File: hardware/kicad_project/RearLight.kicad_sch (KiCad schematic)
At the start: 54 parts, among them J1 USB_C_Receptacle_USB2.0_16P, J2 Conn_02x03_Odd_Even, Q1 CSD16404Q5A, Q2 CSD16404Q5A, U1 453-00039R, U2 USBLC6-2SC6, U3 NPM1100-CAAB-R, U4 DW01A, U5 LIS3DH, U6 OPT3001DNPR, U8 PAM2804AAB010

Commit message: Schematic done; Layout first draft
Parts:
- removed BT1: Battery_Cell, symbol Device:Battery_Cell
- removed D1: L0805G, Capacitor_SMD:C_0805_2012Metric_Pad1.18x1.45mm_HandSolder, symbol Device:LED
- removed D2: L0805R, Capacitor_SMD:C_0805_2012Metric_Pad1.18x1.45mm_HandSolder, symbol Device:LED
- removed D3: XPEBRD-L1, LED_SMD:LED_Cree-XP, symbol RearLight:XPEBRD-L1-0000-00901
- removed MH1, MH2, MH3, MH4: M3, MountingHole:MountingHole_3.2mm_M3_Pad_Via, symbol Mechanical:MountingHole_Pad
- removed Q1, Q2: CSD16404Q5A, Package_TO_SOT_SMD:TDSON-8-1, symbol Transistor_FET:CSD16404Q5A
- removed R16: 2, Resistor_SMD:R_0603_1608Metric, symbol Device:R
- removed R17, R18: 1, Resistor_SMD:R_0603_1608Metric, symbol Device:R
- removed U3: NPM1100-CAAB-R, RearLight:BGA25C40P5X5_207X207X52N, symbol RearLight:NPM1100-CAAB-R
- added BT1: 1096, RearLight:BAT_1096_holes_slim, symbol RearLight:1096
- added C15: 100n, Capacitor_SMD:C_0805_2012Metric, symbol Device:C
- added H1, H2, H3, H4: M2, MountingHole:MountingHole_2.1mm, symbol Mechanical:MountingHole
- added LED1: XPEBRD-L1-0000-00801, RearLight:XPEWHTL1000000E01, symbol RearLight:XPEBRD-L1-0000-00801
- added LED2: LTRB_RASF.01-6B6C-C3E6-0-0-R18, RearLight:LTRBRASF016B6CC3E600R18, symbol RearLight:LTRB_RASF.01-6B6C-C3E6-0-0-R18
- added Q1, Q3: AO3400A, Package_TO_SOT_SMD:SOT-23, symbol Transistor_FET:AO3400A
- added R10: 49R9, Resistor_SMD:R_0402_1005Metric, symbol Device:R
- added R19: 100, Resistor_SMD:R_0402_1005Metric, symbol Device:R
- added R9: 0R1, Resistor_SMD:R_1206_3216Metric, symbol Device:R
- added SW1: SW_Push, RearLight:SW_TS-1088-AR02016, symbol Switch:SW_Push
- added U7: NPM1100-QDAB-R, RearLight:QFN50P400X400X90-25N-D, symbol RearLight:NPM1100-QDAB-R
- C1: Manufacturer Part Number CL21A475KAQNNNE -> (none); manf# (none) -> CL21A475KAQNNNE
- C10, C11, C13, C14, C8, C9: Manufacturer Part Number CL21A106KAYNNNE -> (none); manf# (none) -> CL21A106KAYNNNE
- C12, C5, C6, C7: Manufacturer Part Number CL21B104KCFNNNE -> (none); manf# (none) -> CL21B104KCFNNNE
- C2, C3: Manufacturer Part Number CL10B474KA8NNNC -> (none); manf# (none) -> CL10B474KA8NNNC
- C4: Manufacturer Part Number CL21A225KBQNNNE -> (none); manf# (none) -> CL21A225KBQNNNE
- J1: footprint Connector_USB:USB_C_Receptacle_GCT_USB4105-xx-A_16P_TopMnt_Horizontal -> Connector_USB:USB_C_Receptacle_GCT_USB4105-xx-A_16P_TopMnt_Horizontal_wide_slot; Distribution Link 1 (none) -> https://jlcpcb.com/partdetail/3554049-USB4105_GF_A060/C3025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; LCSC (none) -> C3025063; Manufacturer (none) -> Global Connector Technology; Manufacturer Part Number (none) -> USB4105-GF-A-060; manf# (none) -> USB4105-GF-A-060; now left out of the parts list
- J2: now not fitted
- L1, L2: Manufacturer Part Number CMI201209U2R2KT -> (none); manf# (none) -> CMI201209U2R2KT
- R1, R5: Manufacturer Part Number 0603WAF0000T5E -> (none); manf# (none) -> 0603WAF0000T5E
- R11: Distribution Link 1 https://eu.mouser.com/ProductDetail/Royalohm/0603WAF0000T5E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 -> https://jlcpcb.com/partdetail/26547-0603WAF1002T5E/C25804; Distribution Link 2 https://www.lcsc.com/product-detail/C21189.html -> (none); LCSC C21189 -> C25804; manf# (none) -> 0603WAF1002T5E
- R12, R13, R14, R2, R6: footprint Resistor_SMD:R_0603_1608Metric -> Resistor_SMD:R_0402_1005Metric; Distribution Link 1 https://eu.mouser.com/ProductDetail/Royalohm/0603WAF0000T5E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 -> https://jlcpcb.com/partdetail/26487-0402WGF1002TCE/C25744; Distribution Link 2 https://www.lcsc.com/product-detail/C21189.html -> (none); LCSC C21189 -> C25744; Manufacturer Part Number 0603WAF1002T5E -> 0402WGF1002TCE; manf# (none) -> 0402WGF1002TCE
- R15: value 1 -> 0R1; footprint Resistor_SMD:R_0603_1608Metric -> Resistor_SMD:R_1206_3216Metric; Distribution Link 1 https://www.mouser.com/ProductDetail/Royalohm/0603WAF100KT5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 -> https://jlcpcb.com/partdetail/26077-1206W4F100LT5E/C25334; Distribution Link 2 https://www.lcsc.com/product-detail/C22936.html -> (none); LCSC C22936 -> C25334; Manufacturer Part Number 0603WAF100KT5E -> 1206W4F100LT5E; manf# (none) -> 1206W4F100LT5E
- R3: footprint Resistor_SMD:R_0603_1608Metric -> Resistor_SMD:R_0402_1005Metric; Distribution Link 1 https://jlcpcb.com/partdetail/23906-0603WAF4700T5E/C23179 -> https://jlcpcb.com/partdetail/25860-0402WGF4700TCE/C25117; Distribution Link 2 https://www.lcsc.com/product-detail/C23179.html?s_z=n_C23179 -> (none); Manufacturer Part Number 0603WAF4700T5E -> 0402WGF4700TCE; manf# (none) -> 0402WGF4700TCE
- R4: footprint Resistor_SMD:R_0603_1608Metric -> Resistor_SMD:R_0402_1005Metric; Distribution Link 1 https://www.lcsc.com/product-detail/C22975.html?s_z=n_C22975 -> https://jlcpcb.com/partdetail/4516-0402WGF2001TCE/C4109; Distribution Link 2 https://jlcpcb.com/partdetail/23702-0603WAF2001T5E/C22975 -> (none); LCSC C22975 -> C4109; Manufacturer Part Number 0603WAF2001T5E -> 0402WGF2001TCE; manf# (none) -> 0402WGF2001TCE
- R7, R8: footprint Resistor_SMD:R_0603_1608Metric -> Resistor_SMD:R_0402_1005Metric; LCSC C23186 -> C25905; Manufacturer Part Number 0603WAF5101T5E -> 0402WGF5101TCE; manf# (none) -> 0402WGF5101TCE
- U1: footprint RF_Module:Laird_BL653 -> Liard_BL653_ 453-00039_Custom:Laird_BL653; manf# (none) -> 453-00039R
- U4: Manufacturer Part Number DW01A -> (none); manf# (none) -> DW01A
- U5: Manufacturer Part Number LIS3DHTR -> (none); manf# (none) -> LIS3DHTR
- U6: Manufacturer Part Number OPT3001DNPR -> (none); manf# (none) -> OPT3001DNPR
- U8: Manufacturer Part Number PAM2804AAB010 -> (none); manf# (none) -> PAM2804AAB010
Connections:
- net +BATT: now also C14.1, U8.4 (VIN), BT1.P, U7.15 (VBAT)
- net +VBUS_FIL: now also U7.17 (VBUS)
- net +VDD_nRF: now also LED2.3 (A_BLUE), R10.1, R19.1, U7.1 (VOUTB); no longer C14.1, U8.4 (VIN)
- net +VSYS: now also U7.16 (VSYS), U7.2 (VOUTBSET1), U7.5 (ISET), U7.9 (VTERMSET); no longer C8.1
- net GND: now also C15.2, LED1.3 (THERMAL_PAD), Q1.2 (S), SW1.2, U7.11 (SHPHLD), U7.19 (D-), U7.23 (PVSS), U7.25 (AVSS), U7.3 (VOUTBSET0), U7.4 (AVSS), U7.6 (SHPACT), U7.7 (MODE)
- net I2C_SCL: now also R12.2; no longer R14.2
- net I2C_SDA: now also R14.2; no longer R12.2
- net at U8.5 (VOUT/FB): now also LED1.1 (K), R9.1; no longer R15.1
- net at C13.1, L2.1: now also LED1.2 (A)
- net at U4.3 (OC): now also Q1.1 (G)
- net at C7.1, R6.2, U1.19 (nRESET): now also J2.3 (Pin_3); no longer J2.4 (Pin_4)
- net at R5.1: now also U7.12 (ICHG)
- net RGB_B: now reaches U1.22 (SIO_14)
- net RGB_B: now also LED2.4 (K_BLUE)
- net RGB_R: now reaches U1.27 (SIO_11)
- net RGB_R: now also LED2.5 (K_RED)
- net RGB_G: now reaches U1.28 (SIO_12)
- net RGB_G: now also LED2.6 (K_GREEN)
- net at U1.59 (NFC1/SIO_09): now also U8.1 (EN)
- net ERR_SIG: now reaches U1.63 (SIO_38)
- net ERR_SIG: now also U7.10 (ERR)
- net CHG_SIG: now reaches U1.64 (SIO_39)
- net CHG_SIG: now also U7.8 (CHG); no longer U8.1 (EN)
- net SWITCH: now reaches U1.7 (SIO_32)
- net SWITCH: now also C15.1, SW1.1
- net at C5.2, U4.6 (GND): now also BT1.N, Q3.2 (S)
- net at L1.2: now also U7.22 (SW)
- net at R2.1: now also U7.14 (NTC)
- net at U4.1 (OD): now also Q3.1 (G)
- new net: R15.1, R9.2
- new net: C8.1, U7.21 (DEC)
- new net: Q1.3 (D), Q3.3 (D)
- new net: LED2.1 (A_GREEN), R10.2
- new net: LED2.2 (A_RED), R19.2
- no-connect marks 51 -> 44
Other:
- note added: "I_LED = 0.1/R_s 0.2 Ω equivalent to get 500mA"
- note removed: "0.285 Ω equivalent to get 350mA"
- note removed: "Unpopulated"
- moved on the sheet: C10, C13, C14, C5, C9, L2, R3, R4, U4, U8

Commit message: Layout 2nd draft
Todo: increase via size
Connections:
- net GND: no longer U1.33 (GND), U1.47 (GND)
- no-connect marks 44 -> 47
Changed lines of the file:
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@@
-	)
-	(junction
-		(at 157.48 124.46)
-		(diameter 0)
-		(color 0 0 0 0)
 	)
 	(junction
@@
 	)
 	(junction
-		(at 165.1 124.46)
-		(diameter 0)
-		(color 0 0 0 0)
-	)
-	(junction
 		(at 273.05 101.6)
 		(diameter 0)
@@
 	)
 	(no_connect
+		(at 157.48 121.92)
+	)
+	(no_connect
 		(at 109.22 96.52)
 	)
@@
 	)
 	(no_connect
+		(at 165.2246 121.92)
+	)
+	(no_connect
 		(at 182.88 99.06)
 	)
@@
 	)
 	(no_connect
+		(at 182.88 73.66)
+	)
+	(no_connect
 		(at 147.32 121.92)
 	)
@@
 	(wire
 		(pts
-			(xy 165.1 124.46) (xy 165.1 121.92)
-		)
-		(stroke
-			(width 0)
-			(type default)
-		)
-	)
-	(wire
-		(pts
 			(xy 134.62 124.46) (xy 137.16 124.46)
 		)
@@
 	(wire
 		(pts
-			(xy 157.48 124.46) (xy 157.48 121.92)
-		)
-		(stroke
-			(width 0)
-			(type default)
-		)
-	)
-	(wire
-		(pts
 			(xy 265.43 36.83) (xy 269.24 36.83)
 		)
@@
 	(wire
 		(pts
-			(xy 165.1 124.46) (xy 167.64 124.46)
-		)
-		(stroke
-			(width 0)
-			(type default)
-		)
-	)
-	(wire
-		(pts
 			(xy 52.07 64.77) (xy 57.15 64.77)
 		)
@@
 	(wire
 		(pts
-			(xy 157.48 124.46) (xy 160.02 124.46)
-		)
-		(stroke
-			(width 0)
-			(type default)
-		)
-	)
-	(wire
-		(pts
 			(xy -44.45 57.15) (xy -44.45 59.69)
 		)
@@
 	(wire
 		(pts
-			(xy 162.56 124.46) (xy 165.1 124.46)
-		)
-		(stroke
-			(width 0)
-			(type default)
-		)
-	)
-	(wire
-		(pts
-			(xy 154.94 124.46) (xy 157.48 124.46)
-		)
-		(stroke
+			(xy 162.56 124.46) (xy 167.64 124.46)
+		)
+		(stroke
+			(width 0)
+			(type default)
+		)
+	)
+	(wire
+		(pts
+			(xy 154.94 124.46) (xy 160.02 124.46)
+		)
+		(stroke

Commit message: DFM design overhaul
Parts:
- removed LED2: LTRB_RASF.01-6B6C-C3E6-0-0-R18, RearLight:LTRBRASF016B6CC3E600R18, symbol RearLight:LTRB_RASF.01-6B6C-C3E6-0-0-R18
- removed R19: 100, Resistor_SMD:R_0402_1005Metric, symbol Device:R
- added D1: LED_R, LED_SMD:LED_0603_1608Metric, symbol Device:LED
- added D2: LED_Y, LED_SMD:LED_0805_2012Metric, symbol Device:LED
- added R16: 49R9, RearLight:R_0402_1005Metric_NO_SILK, symbol Device:R
- BT1, U2, U7: now not fitted; now left out of the parts list
- C2, C3: footprint Capacitor_SMD:C_0603_1608Metric -> RearLight:C_0603_1608Metric_NO_SILK
- FID1, FID2, FID3, H1, H2, H3, H4, J1: now not fitted
- R1, R11, R5: footprint Resistor_SMD:R_0603_1608Metric -> RearLight:R_0603_1608Metric_NO_SILK
- R10, R12, R13, R14, R2, R4, R6, R7, R8: footprint Resistor_SMD:R_0402_1005Metric -> RearLight:R_0402_1005Metric_NO_SILK
- R3: footprint Resistor_SMD:R_0402_1005Metric -> RearLight:R_0402_1005Metric_NO_SILK; LCSC C23179 -> C25117
- U1: footprint Liard_BL653_ 453-00039_Custom:Laird_BL653 -> RF_Module:Laird_BL653; now not fitted; now left out of the parts list
- U5: LCSC (none) -> C15134; Manufacturer Part Number (none) -> LIS3DHTR; now not fitted; now left out of the parts list
- U6: Manufacturer Part Number (none) -> OPT3001DNPR
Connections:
- net RGB_G is gone; now on net RGB_R: U1.28 (SIO_12)
- net +VDD_nRF: now also R16.1
- net RGB_R: now also D1.1 (K); no longer U1.27 (SIO_11)
- net at R10.2: now also D1.2 (A)
- net RGB_B: no longer names the net of U1.22 (SIO_14)
- new net: D2.2 (A), R16.2
- new net RGB_Y: D2.1 (K), U1.27 (SIO_11)
- no-connect marks 47 -> 48

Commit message: Added correct tooling holes for JLCPCB assembly
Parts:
- H1, H2, H3, H4: value M2 -> JLCPCB Tooling Hole; footprint MountingHole:MountingHole_2.1mm -> MountingHole:ToolingHole_1.152mm
- LED1, U6, U8: now not fitted; now left out of the parts list
- U7: LCSC C6134668 -> C5833729; now fitted; now in the parts list
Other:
- moved on the sheet: FID1, FID2, FID3, H1

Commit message: better placement & silkscreen for DFM
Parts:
- added 2V7, SCL1, SDA1, VBUS1: TestPoint, TestPoint:TestPoint_Pad_D1.0mm, symbol Connector:TestPoint
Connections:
- net +VBUS_FIL: now also VBUS1.1
- net +VDD_nRF: now also 2V7.1
- net I2C_SCL: now also SCL1.1
- net I2C_SDA: now also SDA1.1

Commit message: Added 100k pulldown to LED driver EN
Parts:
- added R17: 100k, RearLight:R_0402_1005Metric_NO_SILK, symbol Device:R
- U2: Distribution Link 1 (none) -> https://www.lcsc.com/product-detail/C7519.html?s_z=n_USBLC6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; Distribution Link 2 (none) -> https://www.digikey.de/de/products/detail/stmicroelectronic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; LCSC (none) -> C7519; Manufacturer (none) -> STMicroelectronics; Manufacturer Part Number (none) -> USBLC6-2SC6
- U5: value LIS3DH -> LIS3DHTR
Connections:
- net GND: now also R17.2
- net at U1.59 (NFC1/SIO_09), U8.1 (EN): now also R17.1
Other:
- note added: "Pull down to GND Then EN is not floating LED off by default"

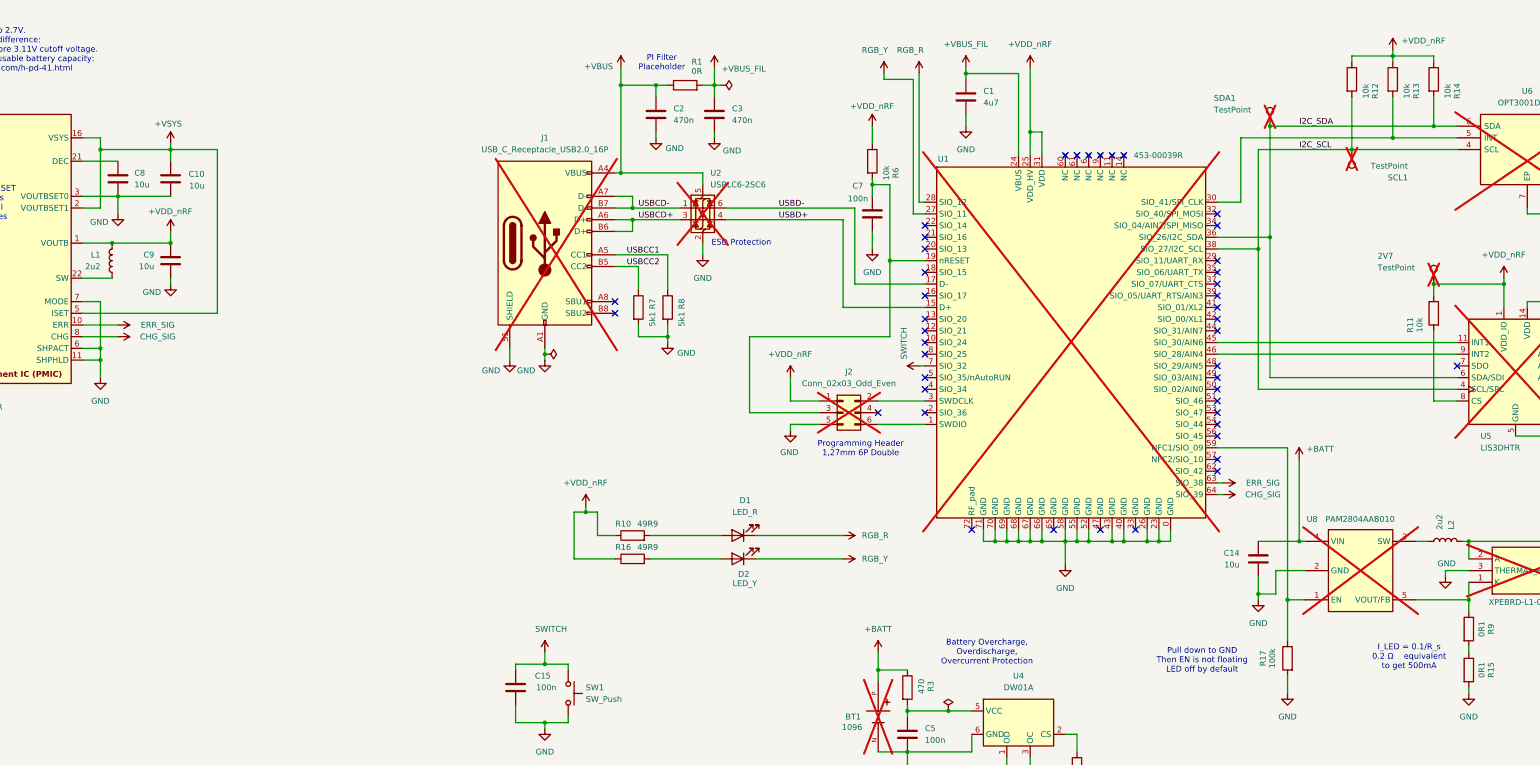
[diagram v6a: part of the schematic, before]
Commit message: Production Version 1.0
Moved red LED to NPM1100
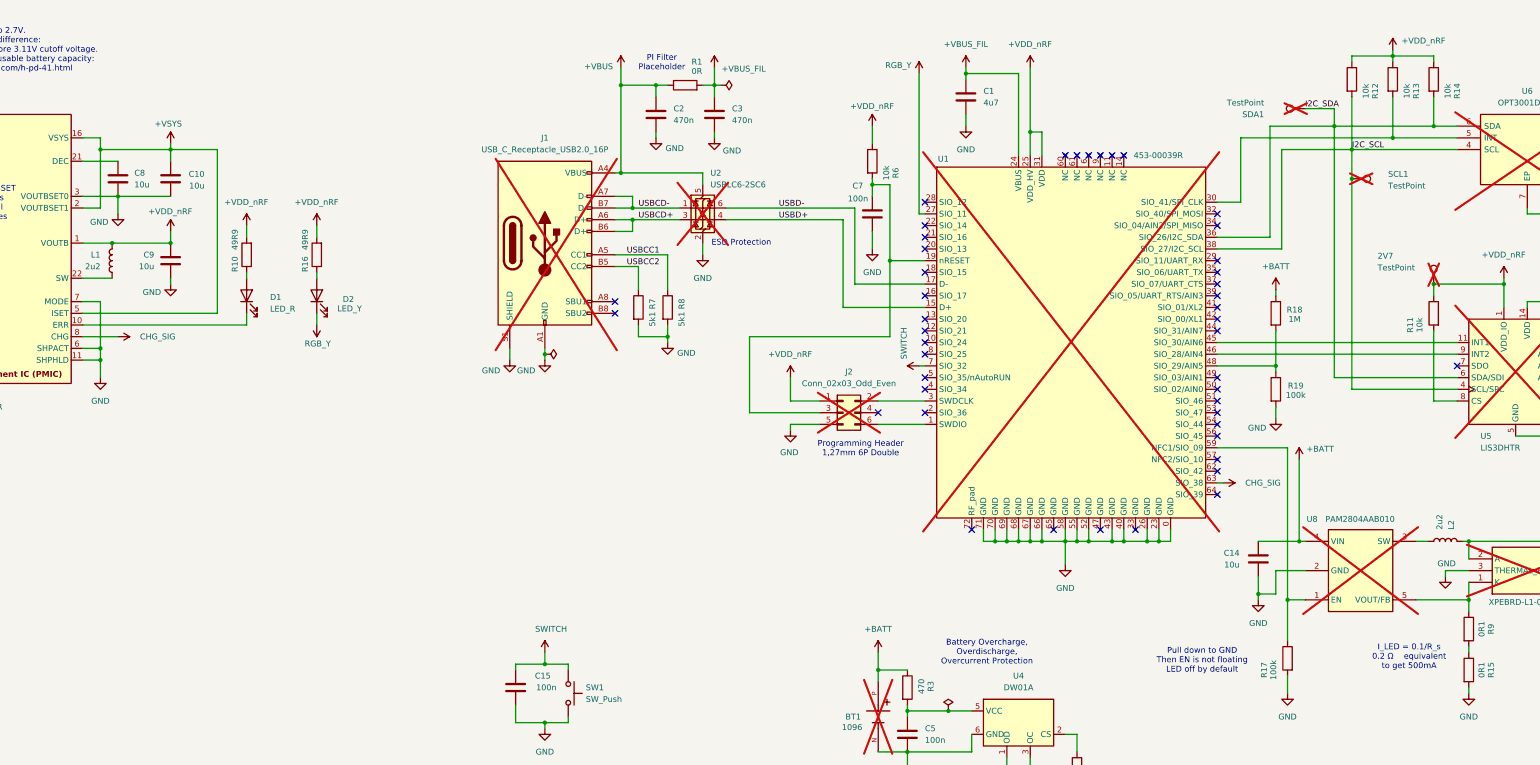
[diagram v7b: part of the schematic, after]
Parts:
- added R18: 1M, RearLight:R_0402_1005Metric_NO_SILK, symbol Device:R
- added R19: 100k, RearLight:R_0402_1005Metric_NO_SILK, symbol Device:R
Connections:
- net +BATT: now also R18.1
- net +VDD_nRF: now also R10.2, R16.2; no longer R10.1, R16.1
- net CHG_SIG: now also U1.63 (SIO_38); no longer U1.64 (SIO_39)
- net GND: now also R19.2
- net at D1.2 (A): now also R10.1; no longer R10.2
- net at D2.2 (A): now also R16.1; no longer R16.2
- net at U1.48 (SIO_29/AIN5): now also R18.2, R19.1
- net ERR_SIG: no longer names the net of U7.10 (ERR)
- net ERR_SIG: now also D1.1 (K); no longer U1.63 (SIO_38)
- net RGB_R: no longer names the net of U1.28 (SIO_12)
- net RGB_R: no longer D1.1 (K)
- no-connect marks 48 -> 49
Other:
- moved on the sheet: D1, D2, R16, SCL1, SDA1

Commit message: updated board thickness to 1.6 mm
The board was manufactured with 1.6 mm board thickness accidentaly.
To reflect this, updated the kicad project as well.
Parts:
- U1: footprint RF_Module:Laird_BL653 -> Liard_BL653_ 453-00039_Custom:Laird_BL653
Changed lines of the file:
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@@
 			)
 		)
-		(property "Footprint" "RF_Module:Laird_BL653"
+		(property "Footprint" "Liard_BL653_ 453-00039_Custom:Laird_BL653"
 			(at 184.404 129.032 0)
 			(effects
